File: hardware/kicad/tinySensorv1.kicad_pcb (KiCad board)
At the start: 2 copper layers, 94 x 60 mm, 30 parts, among them J1 RADIO, J10 CR2032 socket, J11 AAA socket, J12 AA Socket, J13 Bornier, J2 DCDC converter, J3 BMP/BME breakout, J5 OneWire sensor, J6 ISP, J7 Analog sensor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

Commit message: Merge overlapping traces, add a 1n capacitor after DCDC converter
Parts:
- added C5: 1n, Capacitor_THT:CP_Radial_Tantal_D4.5mm_P2.50mm, F.Cu at (155.2, 55.6)
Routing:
- net +3V3: track 179.8 -> 185.8 mm

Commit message: Alpha of pcb version 2
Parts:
- added J4: PWM_OUT, Connector_PinHeader_2.54mm:PinHeader_1x01_P2.54mm_Vertical, F.Cu at (189.7, 65.9)
- C5: moved to B.Cu
- J1, J5, J7: footprint Connector_PinHeader_2.54mm:PinHeader_1x03_P2.54mm_Vertical -> Connector_JST:JST_EH_B03B-EH-A_1x03_P2.50mm_Vertical
- J13: value Bornier -> RAW IN
- moved J6 41.9 mm to (164.0, 85.0), turned to 0 degrees
- moved R2 28.3 mm to (182.4, 77.4)
- moved R3 28.1 mm to (180.0, 77.4), turned to 270 degrees
- moved J1 24.3 mm to (196.0, 52.0)
- moved R6 20.7 mm to (178.0, 55.0)
- moved C3 20.3 mm to (170.0, 51.0), turned to 180 degrees
- moved C4 19.4 mm to (196.0, 57.0), turned to 180 degrees
- moved R4 18.1 mm to (173.0, 54.5)
- moved U1 17.9 mm to (168.9, 70.1), turned to 90 degrees
- moved C2 16.7 mm to (165.5, 64.0), turned to 270 degrees
- moved J5 16.4 mm to (184.0, 52.0)
- moved JP2 14.5 mm to (152.5, 63.0), turned to 180 degrees
- moved J7 13.2 mm to (171.5, 58.5)
- moved C1 9.34 mm to (162.5, 66.0)
- moved J3 8.39 mm to (193.3, 80.0)
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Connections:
- C1 pad 1: +3V3 -> VCC
- C2 pad 2: +3V3 -> VCC
- C4 pad 2: +3V3 -> VCC
- C5 pad 2: +3V3 -> VCC
- J1 pad 2: +3V3 -> VCC
- J2 pad 3: +3V3 -> VCC
- J3 pad 1: +3V3 -> /SENSOR_VCC
- J5 pad 3: +3V3 -> /SENSOR_VCC
- J6 pad 2: +3V3 -> VCC
- J7 pad 3: +3V3 -> /SENSOR_VCC
- JP2 pad 1: +BATT -> VCC
- JP2 pad 2: +3V3 -> +BATT
- R2 pad 1: +3V3 -> /SENSOR_VCC
- R3 pad 1: +3V3 -> /SENSOR_VCC
- R6 pad 1: +3V3 -> /SENSOR_VCC
- U1 pad 1: +3V3 -> VCC
- U1 pad 11: Net-(U1-Pad11) -> /SENSOR_VCC
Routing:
- net +3V3: track 185.8 -> 0.00 mm
- net VCC: track 0.00 -> 106.9 mm
- net /SENSOR_VCC: track 0.00 -> 80.7 mm
- net +BATT: track 194.2 -> 135.5 mm, vias 0 -> 1
- net GND: track 311.9 -> 266.0 mm
- net /SDA: track 63.8 -> 36.0 mm
- net /LED_OUT: track 27.3 -> 6.61 mm
- net /TX_RADIO: track 9.83 -> 29.1 mm
- net /MISO: track 17.3 -> 30.5 mm, vias 0 -> 2
- net /PWM_OUT: track 0.00 -> 9.83 mm
- net /SCL: track 62.3 -> 52.8 mm, vias 0 -> 2
- net /Analog_sensor: track 16.4 -> 8.64 mm
- net /RESET: track 8.62 -> 14.0 mm
- net Net-(C3-Pad1): track 3.30 -> 6.57 mm
- net Net-(JP1-Pad2): track 5.84 -> 8.96 mm
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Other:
- net class power added: clearance 0.2, trace_width 0.3, via_dia 0.8, via_drill 0.4
- board text added: "TinySensor v2.0"

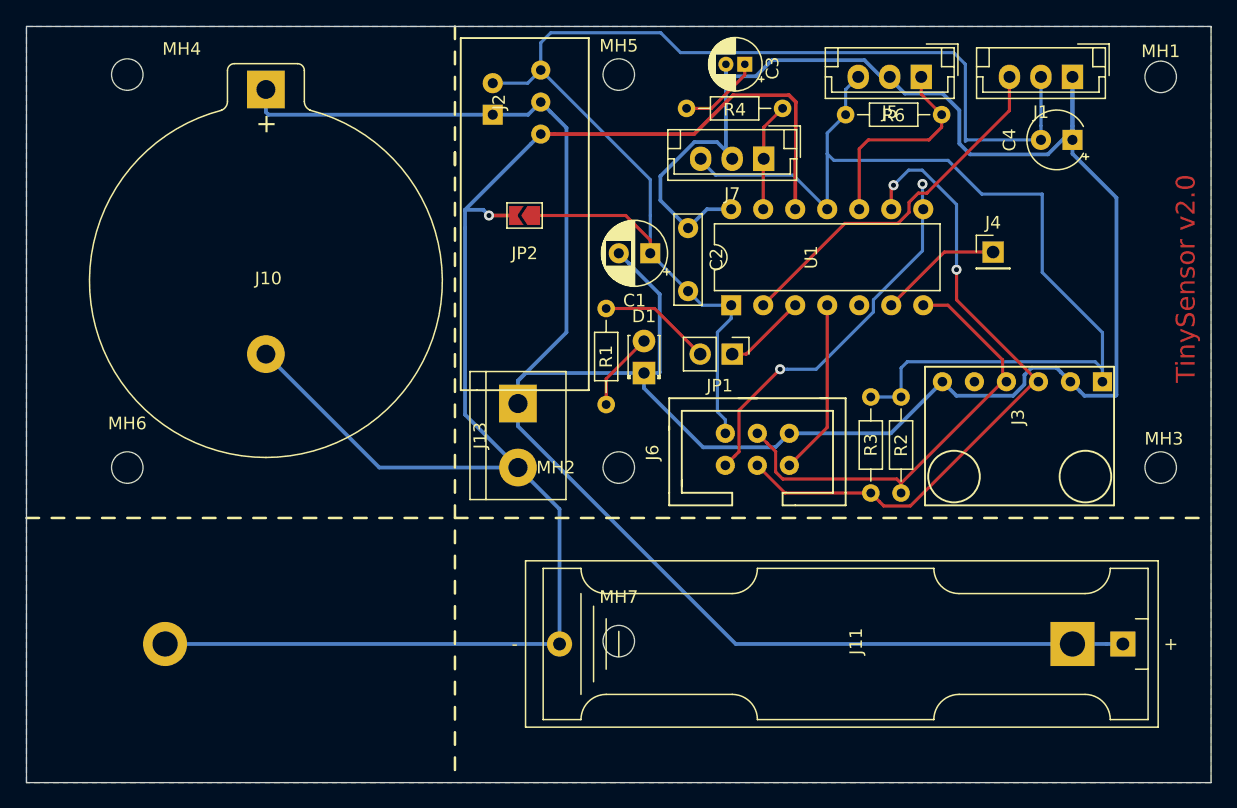
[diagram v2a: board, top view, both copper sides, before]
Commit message: Fix HW bugs around analog sensor and begin radio connector move
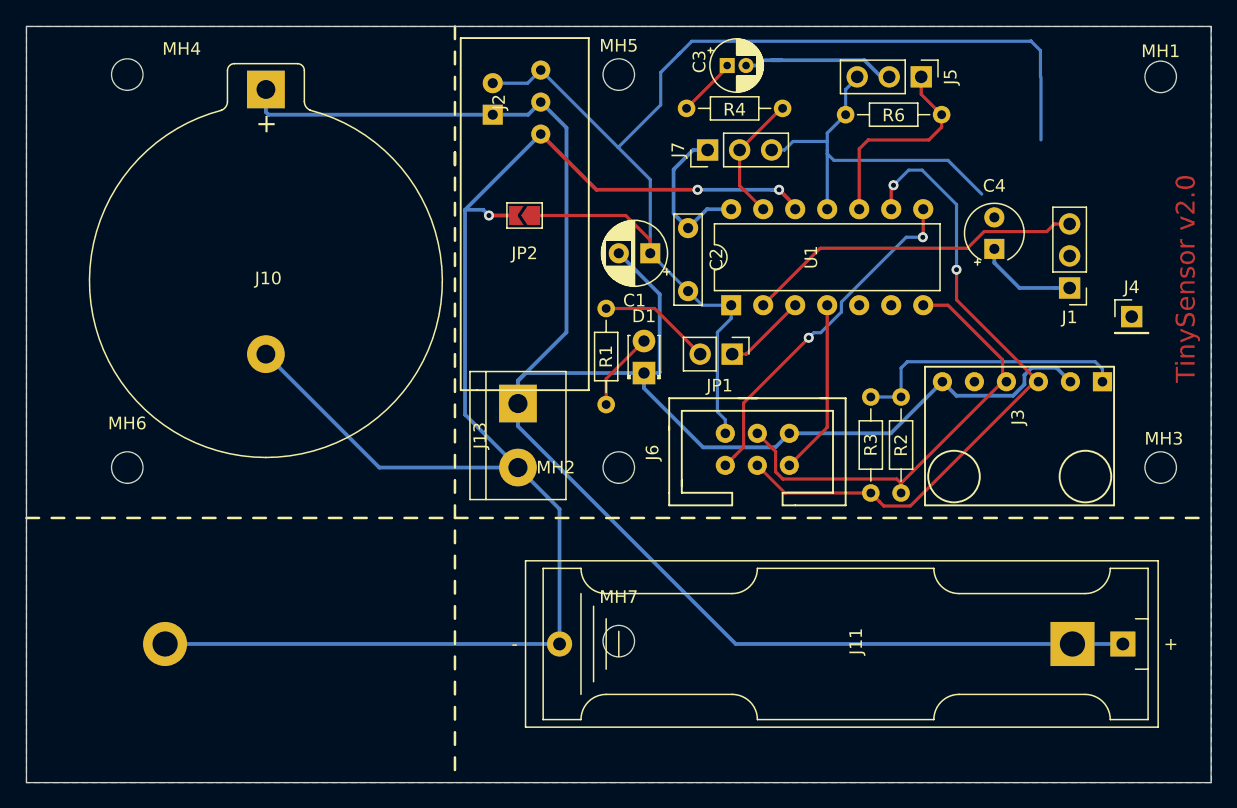
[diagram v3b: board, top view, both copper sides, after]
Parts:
- J1, J5, J7: footprint Connector_JST:JST_EH_B03B-EH-A_1x03_P2.50mm_Vertical -> Connector_PinHeader_2.54mm:PinHeader_1x03_P2.54mm_Vertical
- moved J1 16.8 mm to (195.8, 68.8)
- moved J4 12.1 mm to (200.7, 71.0)
- moved C4 10.6 mm to (189.8, 65.7), turned to 90 degrees
- moved J7 4.50 mm to (167.1, 57.8), turned to 90 degrees
- moved C3 1.40 mm to (168.6, 51.1), turned to 0 degrees
- turned J5 to 270 degrees
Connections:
- J7 pad 1: /Analog_sensor -> GND
- J7 pad 2: GND -> /Analog_sensor
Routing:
- net GND: track 266.0 -> 205.7 mm
- net /SENSOR_VCC: track 80.7 -> 52.0 mm
- net /PWM_OUT: track 9.83 -> 0.00 mm
- net VCC: track 106.9 -> 98.7 mm
- net +BATT: track 135.5 -> 128.1 mm, vias 1 -> 3
- net /MISO: track 30.5 -> 27.9 mm
- net /TX_RADIO: track 29.1 -> 27.0 mm
- net Net-(C3-Pad1): track 6.57 -> 4.73 mm
- net /Analog_sensor: track 8.64 -> 10.3 mm

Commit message: Use new DCDC converter footprint, do no explicitely display GND
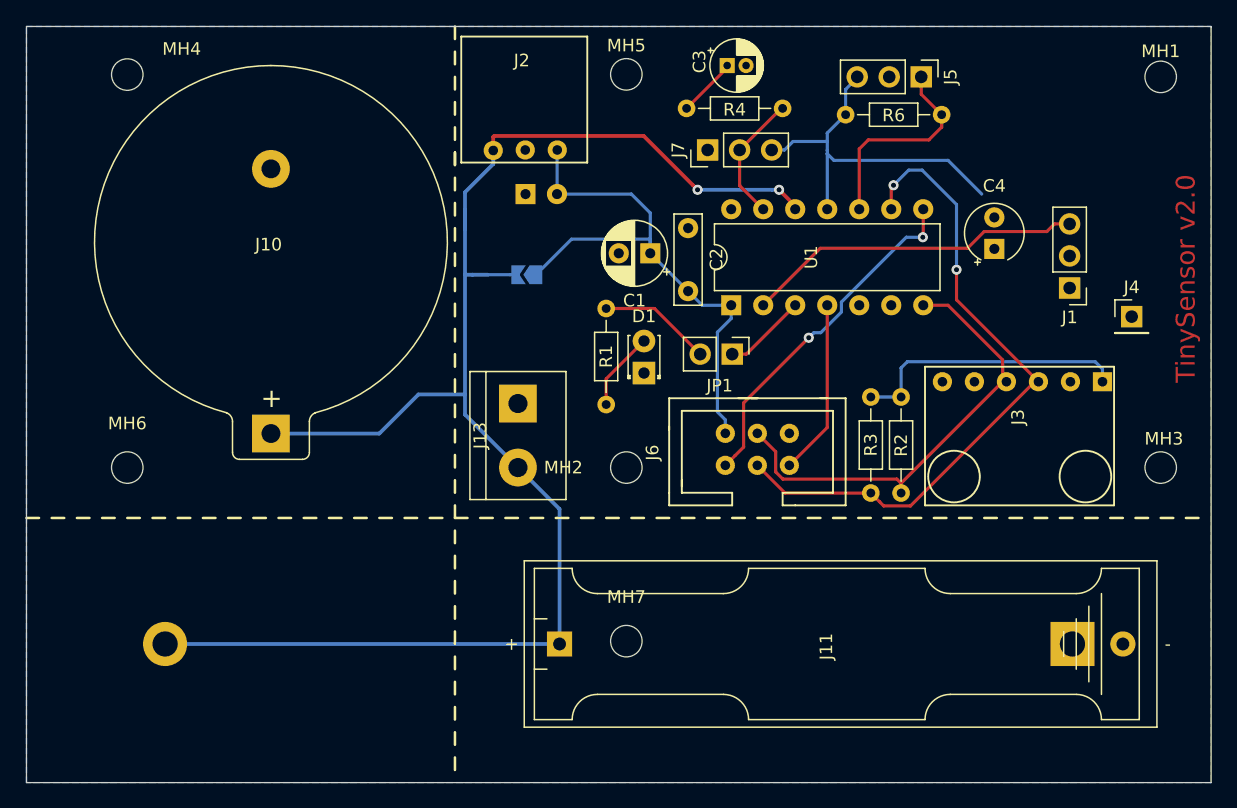
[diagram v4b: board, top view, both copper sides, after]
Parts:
- J2: footprint TinySensor lib:DC-DC_0.9v-3.3v_to_3.3v -> TinySensor lib:DC-DC 0.9v-3.3v to 3v3mini
- JP2: moved to B.Cu
- moved J11 44.7 mm to (155.3, 97.0), turned to 0 degrees
- moved J10 27.3 mm to (132.4, 80.3), turned to 90 degrees
- moved C5 6.82 mm to (152.6, 61.3), turned to 0 degrees
- moved J2 5.41 mm to (147.5, 58.8), turned to 0 degrees
- moved JP2 4.70 mm to (152.7, 67.7)
- moved MH5 0.60 mm to (160.6, 51.8)
- moved MH2 0.60 mm to (160.6, 83.0)
- moved MH7 0.60 mm to (160.6, 96.8)
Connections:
- J10 pad 1: GND -> +BATT
- J10 pad 2: +BATT -> GND
- J11 pad 1: GND -> +BATT
- J11 pad 2: +BATT -> GND
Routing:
- net GND: track 205.7 -> 0.15 mm
- net VCC: track 98.7 -> 45.1 mm
- net +BATT: track 128.1 -> 125.7 mm, vias 3 -> 2
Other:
- net class power removed

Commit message: Update new board and Readme
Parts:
- C4: value 1n -> 10u; footprint Capacitor_THT:CP_Radial_Tantal_D4.5mm_P2.50mm -> Capacitor_THT:CP_Radial_D5.0mm_P2.50mm
- C5: moved to F.Cu
- J2: footprint TinySensor lib:DC-DC 0.9v-3.3v to 3v3mini -> TinySensor lib:DC-DC_0.9v-3.3v_to_3.3v
- J4: value PWM_OUT -> PWM out; footprint Connector_PinHeader_2.54mm:PinHeader_1x01_P2.54mm_Vertical -> Connector_PinHeader_2.54mm:PinHeader_1x02_P2.54mm_Vertical
- moved J1 7.30 mm to (193.0, 62.0)
- moved C4 6.05 mm to (194.0, 70.0), turned to 180 degrees
- moved R1 2.83 mm to (157.0, 76.0)
- moved C3 2.40 mm to (171.0, 51.0)
- moved J4 2.05 mm to (201.0, 69.0)
- moved R4 2.00 mm to (175.0, 54.5)
- moved J7 1.87 mm to (168.9, 57.8)
- moved D1 1.12 mm to (161.0, 75.0)
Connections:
- C4 pad 1: GND -> VCC
- C4 pad 2: VCC -> GND
- J4 pad 1: /PWM_OUT -> GND
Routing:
- net VCC: track 45.1 -> 85.0 mm
- net /PWM_OUT: track 0.00 -> 26.6 mm, vias 0 -> 1
- net /SCL: track 52.8 -> 56.3 mm
- net Net-(JP1-Pad2): track 8.96 -> 11.8 mm
- net +BATT: track 125.7 -> 127.8 mm
- net /SDA: track 36.0 -> 37.7 mm
- net /SENSOR_VCC: track 52.0 -> 53.0 mm, vias 0 -> 2
- net Net-(D1-Pad2): track 6.28 -> 5.47 mm
- net /Analog_sensor: track 10.3 -> 9.61 mm
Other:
- board text added: "Analog sensor"
- board text added: "DC-DC Converter"
- board text added: "Direct Vcc"
- board text added: "OneWire sensor"
- board text added: "PWM out"
- board text added: "Signal output"
- board text added: "i2c sensor"

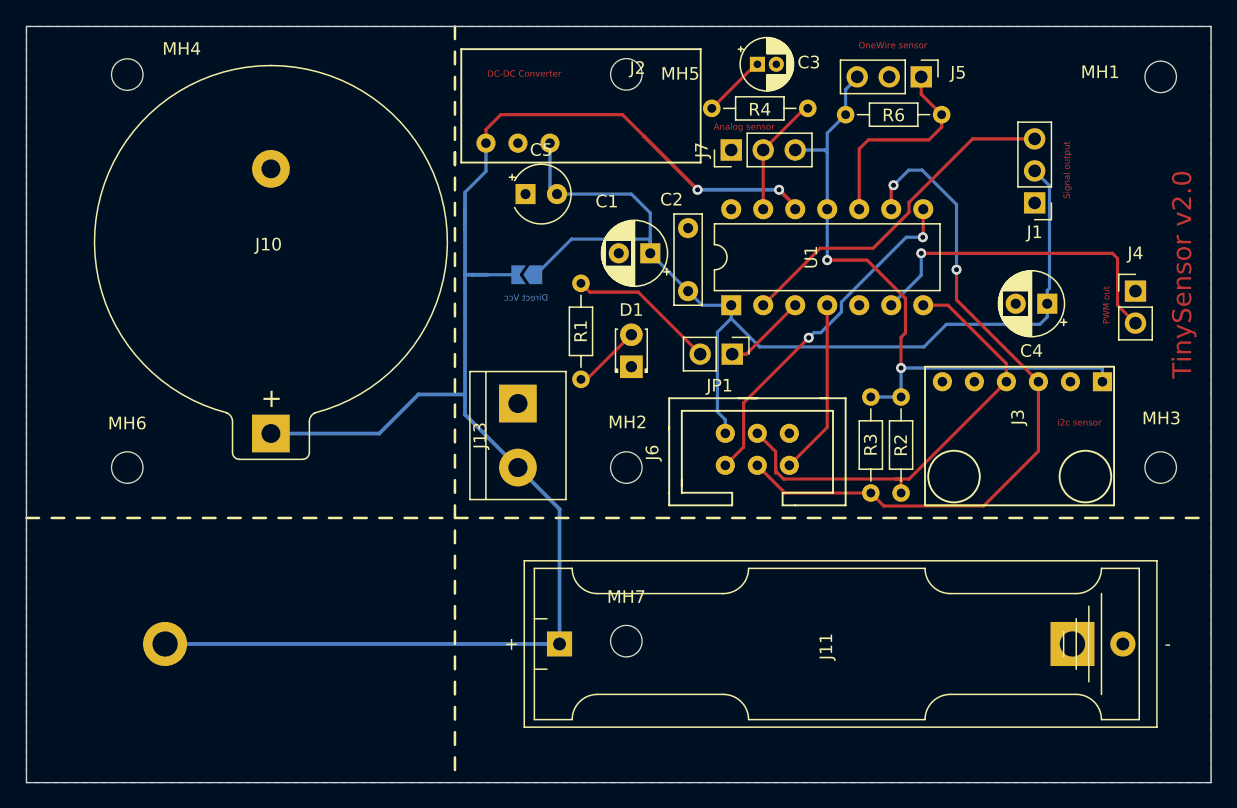
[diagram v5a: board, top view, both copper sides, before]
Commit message: feat: Many updates of PCB
* Fixed many polarity bugs: Vcc is always on the square pad, but
  for 433Mhz emmiter which is somewhat strange
* Added INT0 header
* Allow resistor bridge on analog sensor, to allow usage of LDR
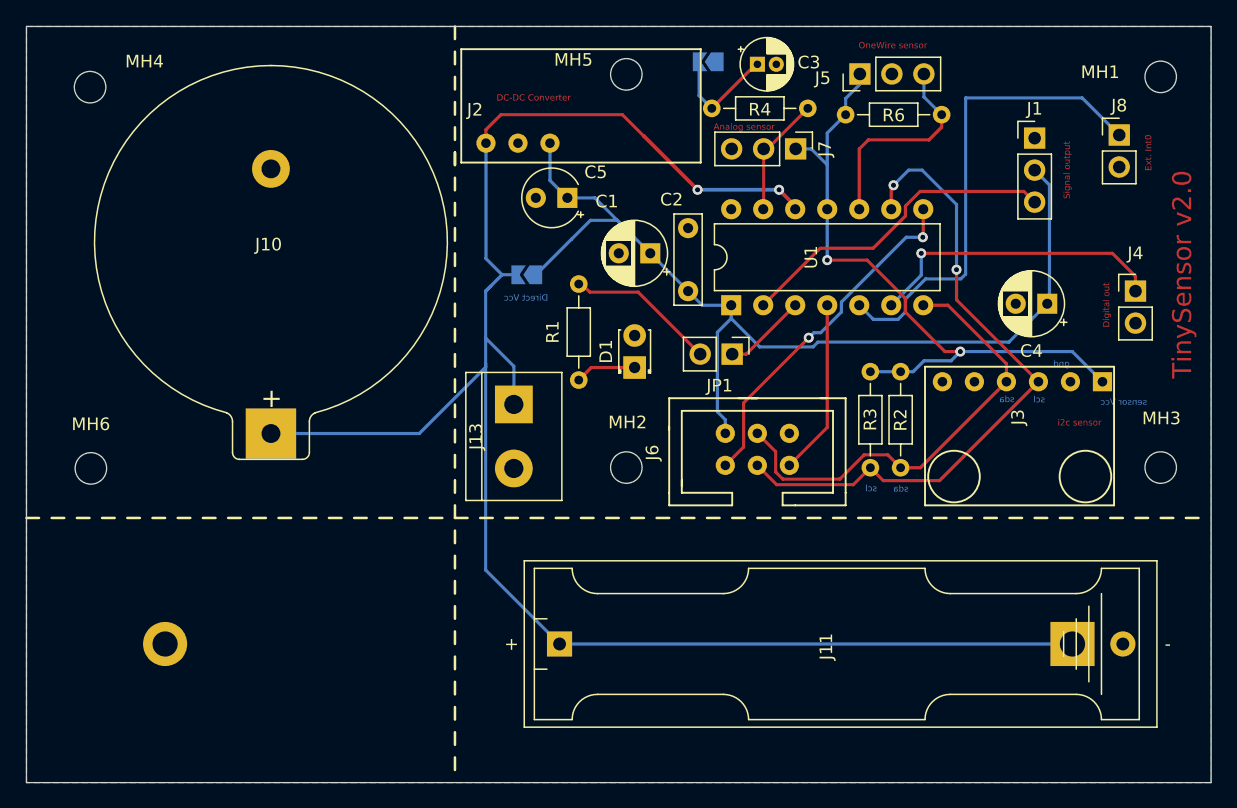
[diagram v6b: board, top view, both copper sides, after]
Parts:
- removed MH7: MountingHole, MountingHole:MountingHole_2.5mm
- added J8: EXT. INT0, Connector_PinHeader_2.54mm:PinHeader_1x02_P2.54mm_Vertical, F.Cu at (199.7, 56.6)
- added JP3: , Jumper:SolderJumper-2_P1.3mm_Open_TrianglePad1.0x1.5mm, B.Cu at (167.1, 50.8)
- J3: value BMP/BME breakout -> I2C Sensor (BME/BMP 280)
- moved J1 5.14 mm to (193.0, 56.9), turned to 0 degrees
- moved J7 5.12 mm to (174.0, 57.7), turned to 270 degrees
- moved J5 4.87 mm to (179.1, 51.8), turned to 90 degrees
- moved C5 3.33 mm to (155.9, 61.6), turned to 180 degrees
- moved MH4 3.12 mm to (118.0, 52.8)
- moved MH6 2.89 mm to (118.1, 83.1)
- moved R2 2.01 mm to (182.4, 75.4)
- moved R3 2.01 mm to (180.0, 75.4)
- moved J13 0.33 mm to (151.7, 78.0)
- moved D1 0.27 mm to (161.3, 75.1)
- moved R1 0.18 mm to (156.8, 76.1)
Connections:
- C5 pad 1: GND -> VCC
- C5 pad 2: VCC -> GND
- D1 pad 1: GND -> Net-(D1-Pad1)
- D1 pad 2: Net-(D1-Pad2) -> GND
- J12 pad 1: GND -> +BATT
- J12 pad 2: +BATT -> GND
- J13 pad 1: GND -> +BATT
- J13 pad 2: +BATT -> GND
- J3 pad 5: Net-(J3-Pad5) -> (no net)
- J4 pad 1: GND -> /PWM_OUT
- J4 pad 2: /PWM_OUT -> GND
- J5 pad 1: /OneWire -> /SENSOR_VCC
- J5 pad 3: /SENSOR_VCC -> /OneWire
- J7 pad 1: GND -> /SENSOR_VCC
- J7 pad 3: /SENSOR_VCC -> GND
- R1 pad 1: Net-(D1-Pad2) -> Net-(D1-Pad1)
- U1 pad 5: Net-(U1-Pad5) -> /INT0
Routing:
- net /INT0: track 0.00 -> 38.4 mm
- net +BATT: track 127.8 -> 140.9 mm
- net Net-(D1-Pad2): track 5.47 -> 0.00 mm
- net VCC: track 85.0 -> 79.8 mm
- net Net-(D1-Pad1): track 0.00 -> 4.88 mm
- net Net-(C3-Pad1): track 5.07 -> 9.19 mm
- net /SCL: track 56.3 -> 52.5 mm
- net /PWM_OUT: track 26.6 -> 24.0 mm
- net /TX_RADIO: track 27.5 -> 26.1 mm
- net /SDA: track 37.7 -> 36.7 mm
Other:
- board text added: "Digital out"
- board text added: "Ext. Int0"
- board text added: "gnd"
- board text added: "scl"
- board text added: "sda"
- board text added: "sensor Vcc"
- board text removed: "PWM out"
